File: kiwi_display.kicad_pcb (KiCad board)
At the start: 2 copper layers, 97.5 x 47.1 mm, 64 parts, among them J1 Conn_01x06, J2 Conn_01x05, Q1 BSS138, Q2 BSS138, Q3 BSS138, U1 TPIC6C595, U2 KCSA02-106, U3 TPIC6C595, U4 KCSA02-106, U5 TPIC6C595, U6 KCSA02-106, U7 TPIC6C595, U8 KCSA02-106

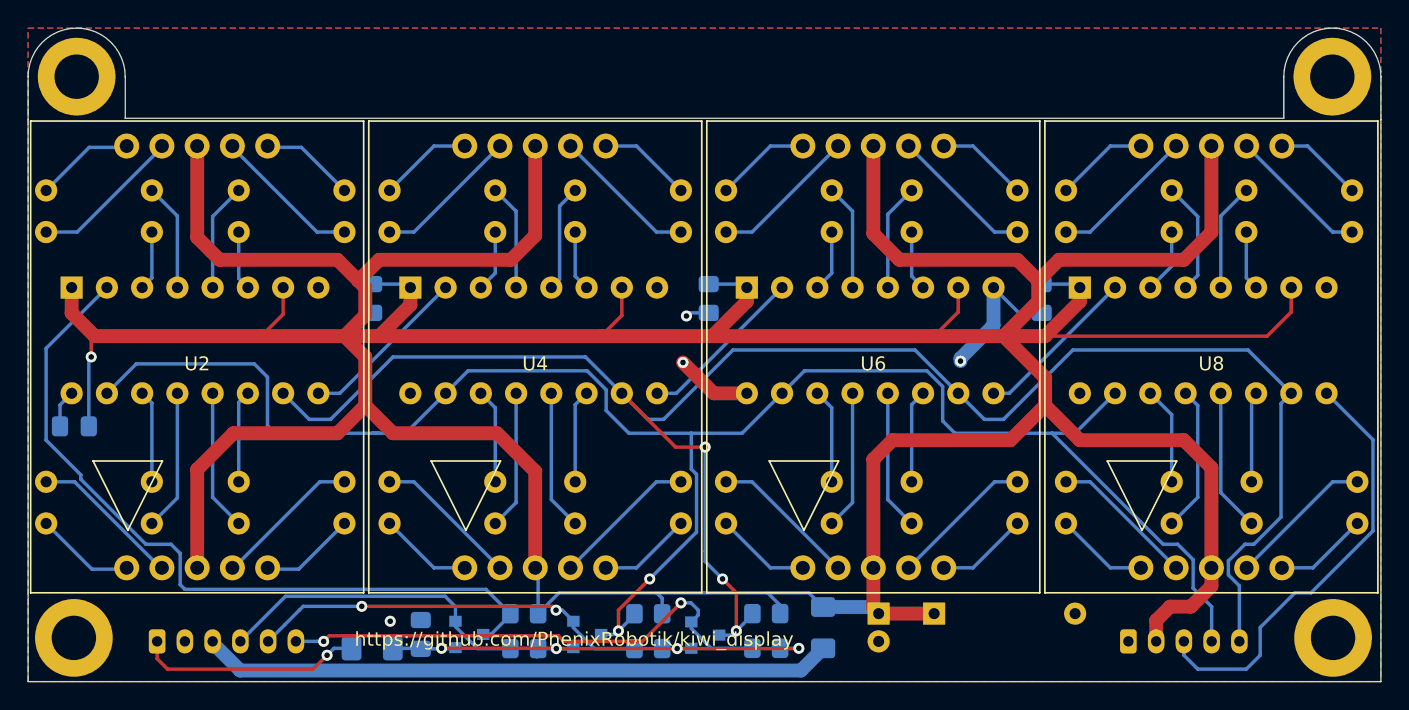
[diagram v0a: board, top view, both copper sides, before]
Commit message: with cms resistors
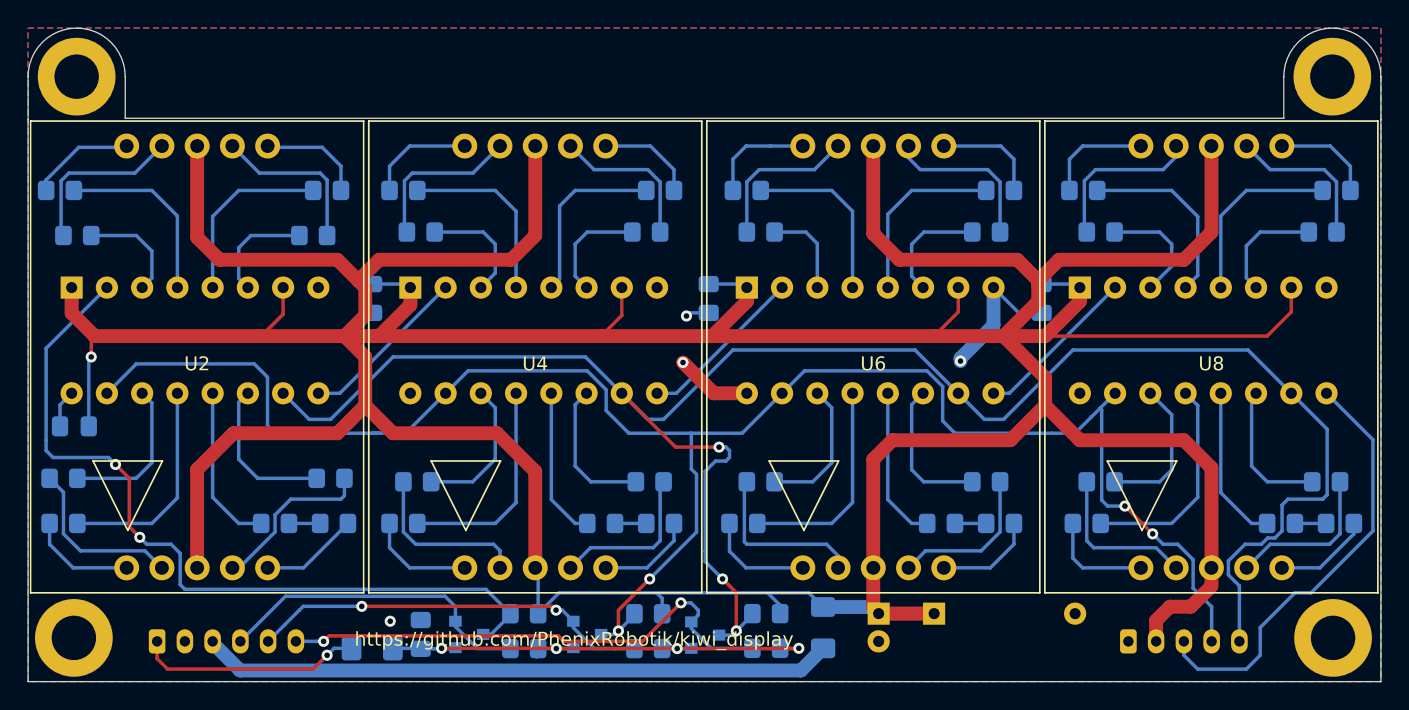
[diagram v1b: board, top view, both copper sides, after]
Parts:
- added R39: 120R, Resistor_SMD:R_0805_2012Metric_Pad1.20x1.40mm_HandSolder, B.Cu at (104.5, 66.0)
- added R40: 120R, Resistor_SMD:R_0805_2012Metric_Pad1.20x1.40mm_HandSolder, B.Cu at (128.0, 66.0)
- added R41: 120R, Resistor_SMD:R_0805_2012Metric_Pad1.20x1.40mm_HandSolder, B.Cu at (152.5, 66.0)
- added R42: 120R, Resistor_SMD:R_0805_2012Metric_Pad1.20x1.40mm_HandSolder, B.Cu at (177.0, 66.0)
- R1, R10, R11, R12, R13, R14, R15, R16, R17, R18, R19, R2, R20, R21, R22, R23, R24, R25, R26, R27, R28, R29, R3, R30, R31, R32, R4, R5, R6, R7, R8, R9: value R -> 120R; footprint Resistor_THT:R_Axial_DIN0207_L6.3mm_D2.5mm_P7.62mm_Horizontal -> Resistor_SMD:R_0805_2012Metric_Pad1.20x1.40mm_HandSolder
- moved R22 2.50 mm to (139.5, 63.0)
- moved R23 2.50 mm to (139.5, 45.0)
- moved R30 2.50 mm to (164.0, 63.0)
- moved R31 2.50 mm to (164.0, 45.0)
- moved R9 2.50 mm to (131.2, 45.0)
- moved R1 2.26 mm to (107.2, 45.2)
- moved R7 2.26 mm to (90.2, 45.2)
- moved R10 2.25 mm to (131.5, 63.0)
- moved R15 2.25 mm to (115.0, 45.0)
- moved R17 2.25 mm to (155.8, 45.0)
- moved R18 2.25 mm to (155.8, 63.0)
- moved R26 2.25 mm to (180.2, 63.0)
- moved R25 2.12 mm to (180.0, 45.0)
- moved R14 2.00 mm to (114.8, 63.0)
- moved R13 1.50 mm to (132.2, 42.0)
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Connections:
- R8 pad 2: Net-(R8-Pad2) -> Net-(R39-Pad1)
- U1 pad 12: Net-(R8-Pad2) -> Net-(R39-Pad2)
- U3 pad 12: Net-(R16-Pad2) -> Net-(R40-Pad2)
- U5 pad 12: Net-(R24-Pad2) -> Net-(R41-Pad2)
- U7 pad 12: Net-(R32-Pad2) -> Net-(R42-Pad2)
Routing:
- net Net-(R39-Pad2): track 0.00 -> 11.8 mm
- net Net-(R42-Pad2): track 0.00 -> 11.4 mm
- net Net-(R41-Pad2): track 0.00 -> 11.2 mm
- net Net-(R40-Pad2): track 0.00 -> 11.0 mm
- net Net-(R8-Pad2): track 10.2 -> 0.00 mm
- net Net-(R32-Pad2): track 10.3 -> 2.25 mm
- net Net-(R24-Pad2): track 10.1 -> 2.25 mm
- net Net-(R16-Pad2): track 10.1 -> 2.25 mm
- net /sheet6191A868/high: track 130.5 -> 137.5 mm
- net Net-(R4-Pad2): track 7.76 -> 13.4 mm
- net Net-(R11-Pad2): track 10.0 -> 15.6 mm
- net Net-(R12-Pad2): track 7.62 -> 13.2 mm
- net Net-(R29-Pad2): track 7.76 -> 13.3 mm
- net Net-(R5-Pad2): track 7.78 -> 13.1 mm
- net Net-(R3-Pad2): track 10.1 -> 15.5 mm
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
